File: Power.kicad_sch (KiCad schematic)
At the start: 64 parts, among them U1 XC7Z020-2CLG484I, U19 LM3880, U20 LM3880, U21 SC189 - 1.0V, U22 SC189 - 3.3V, U23 TLV62080DSGx, U24 SC189 - 1.8V

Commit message: updated layouts, added motor
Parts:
- renumbered C127 to C151, C128 to C152, C129 to C153, C130 to C154, C131 to C155, C132 to C156, C133 to C157, C134 to C158, C135 to C159, C136 to C160, C137 to C161, C138 to C162, C139 to C163, C140 to C164, C141 to C165, C142 to C166, C143 to C167, C144 to C168, C145 to C169, C146 to C170, C147 to C171, C148 to C172, C149 to C173, C150 to C174, C151 to C175, C152 to C176, C153 to C177, C154 to C178, C155 to C179, C156 to C180, C157 to C181, C158 to C182, C159 to C183, C160 to C184, C161 to C185, C162 to C186, C163 to C187, C164 to C188, C165 to C189, R87 to R143, R67 to R144, R88 to R145, R89 to R146, R90 to R147, R91 to R148, R92 to R149, R93 to R150, R94 to R151, R95 to R152, R96 to R153, R97 to R154, U19 to U17, U20 to U18, U21 to U19, U22 to U20, U23 to U21, U24 to U22

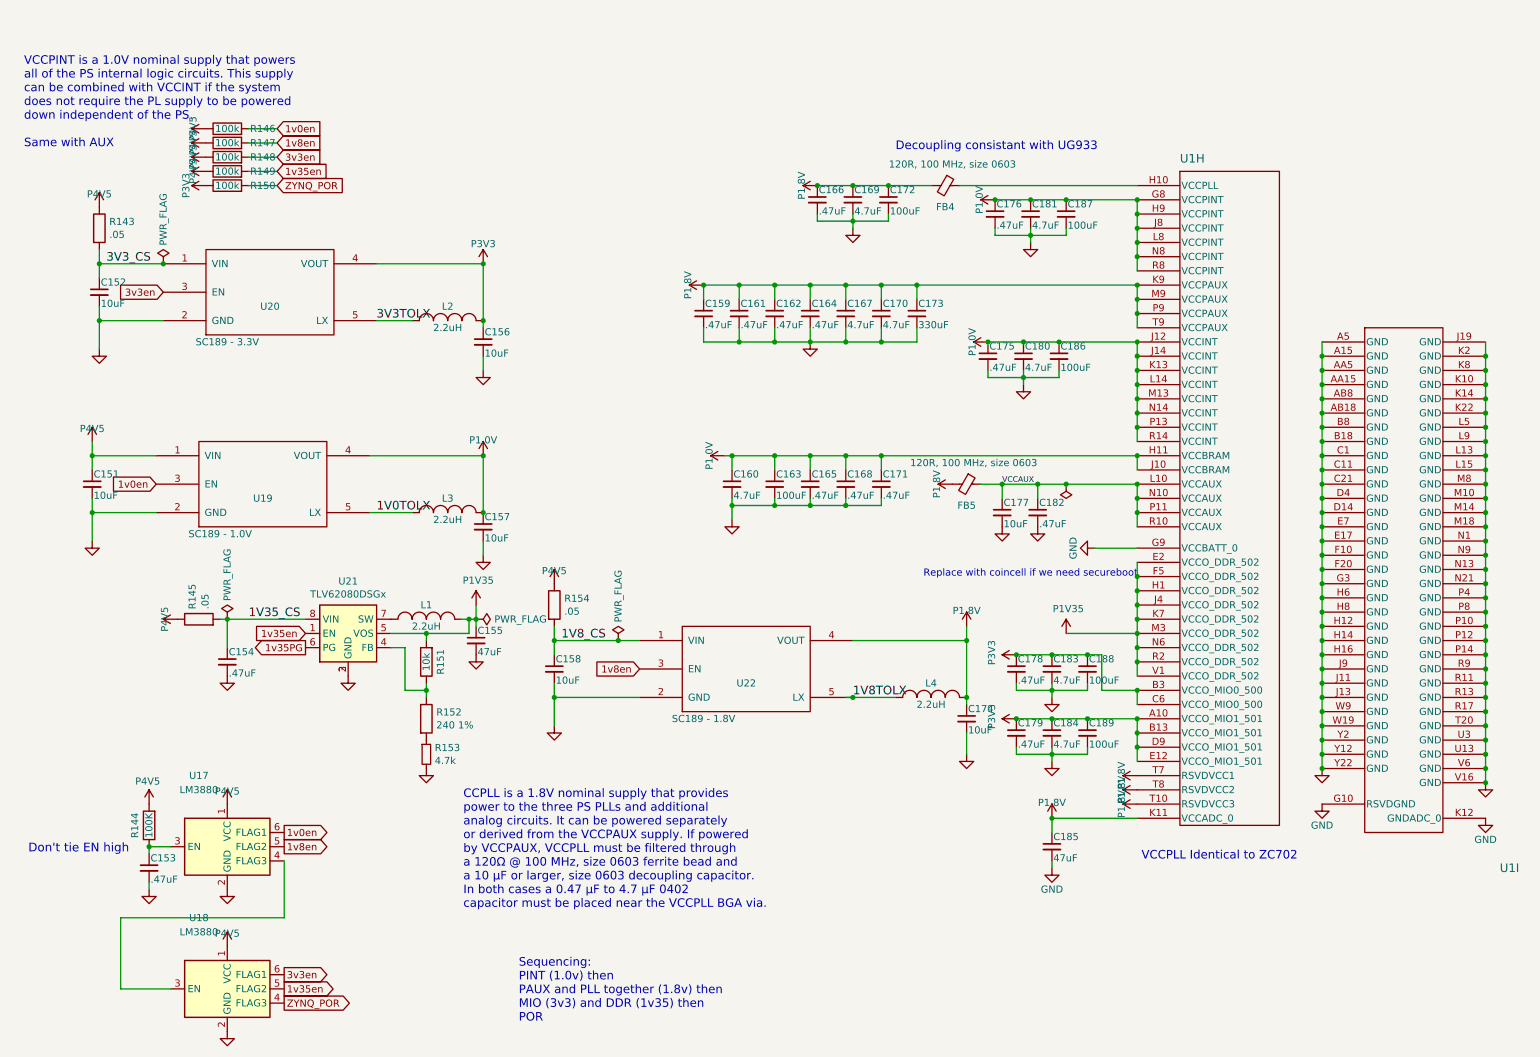
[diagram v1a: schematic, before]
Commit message: Changes to layout pins
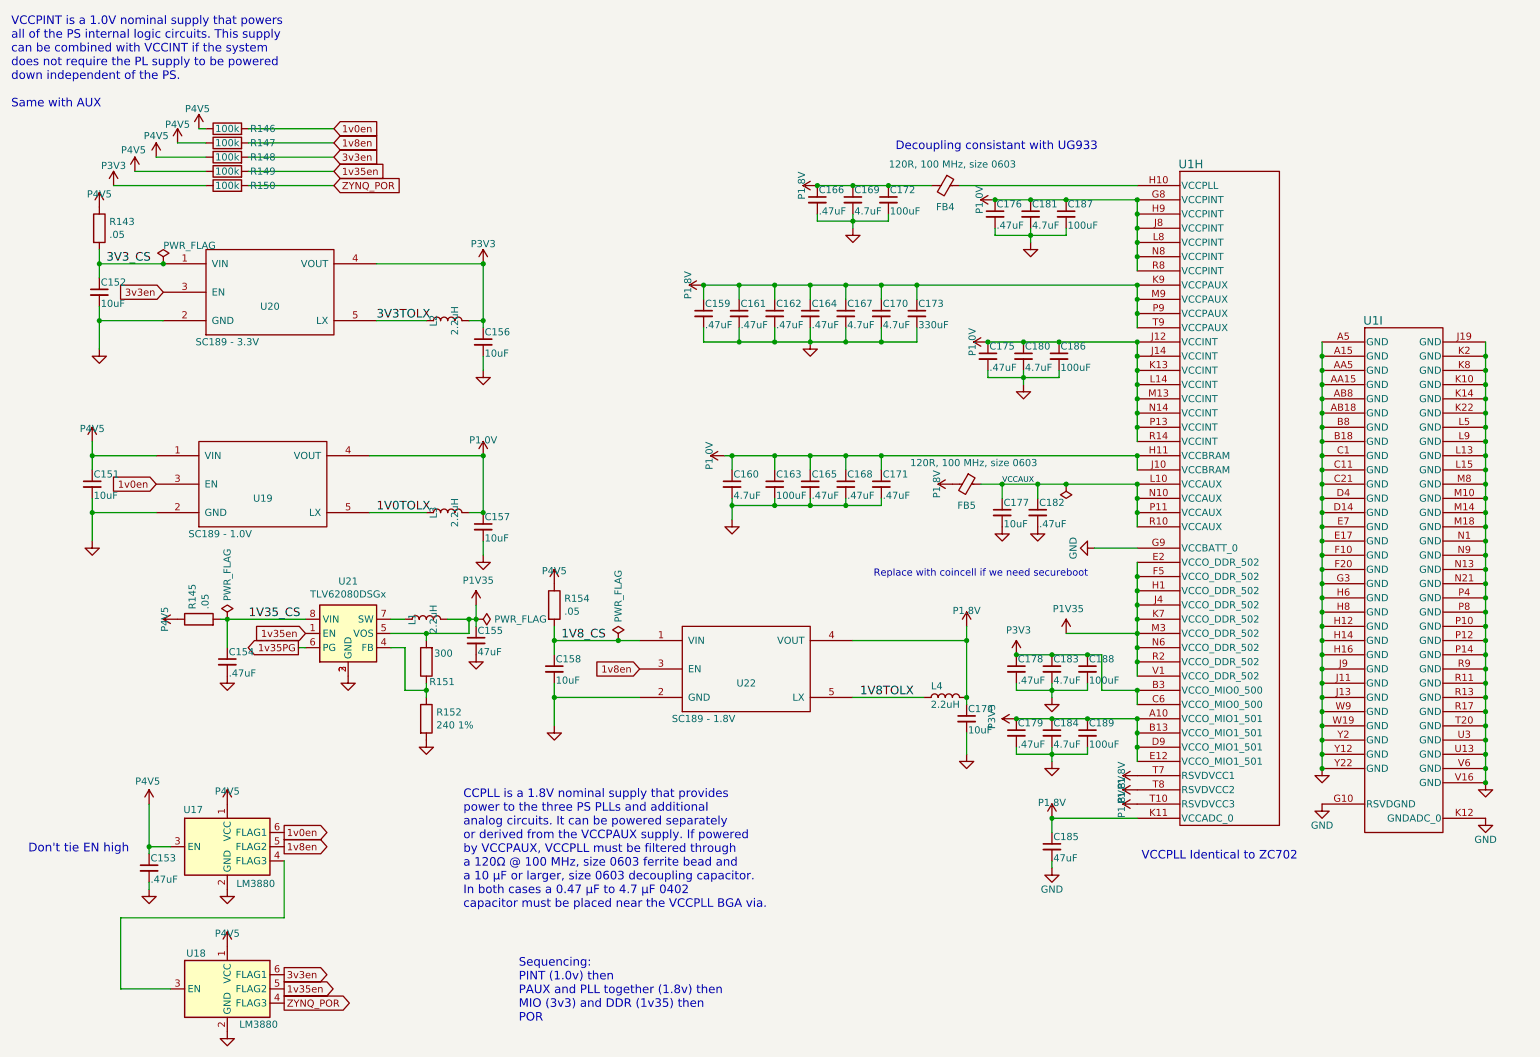
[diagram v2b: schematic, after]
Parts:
- removed R144: 100K, Resistor_SMD:R_0402_1005Metric, symbol Device:R
- removed R153: 4.7k, Resistor_SMD:R_0402_1005Metric, symbol Device:R_Small
- FB4, FB5: symbol Device:Ferrite_Bead_Small -> Device:FerriteBead_Small
- L1, L2, L3, L4: symbol DFTBoard-rescue:INDUCTOR_SMALL_P- -> Device:L
- R143, R145, R154: symbol DFTCustom:R -> Device:R
- R151: value 10k -> 300
- U1: footprint DFTcustom:BGA-484_19.0x19.0mm_Layout22x22_P0.80mm_dia0.40mm -> FPGA:BGA-484_19.0x19.0mm_Layout22x22_P0.80mm_dia0.40mm
- U19, U20, U22: symbol DFTBoard-rescue:SC189- -> KiCAD_Library_Cooter:SC189-
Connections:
- net GND: now also R152.2
- net P4V5: now also C153.1, U17.3 (EN)
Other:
- moved on the sheet: L1, L2, L3, L4
